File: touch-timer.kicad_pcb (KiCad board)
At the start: 2 copper layers, 23 parts, among them Q2 2N3904, U1 WeMos_D1_mini

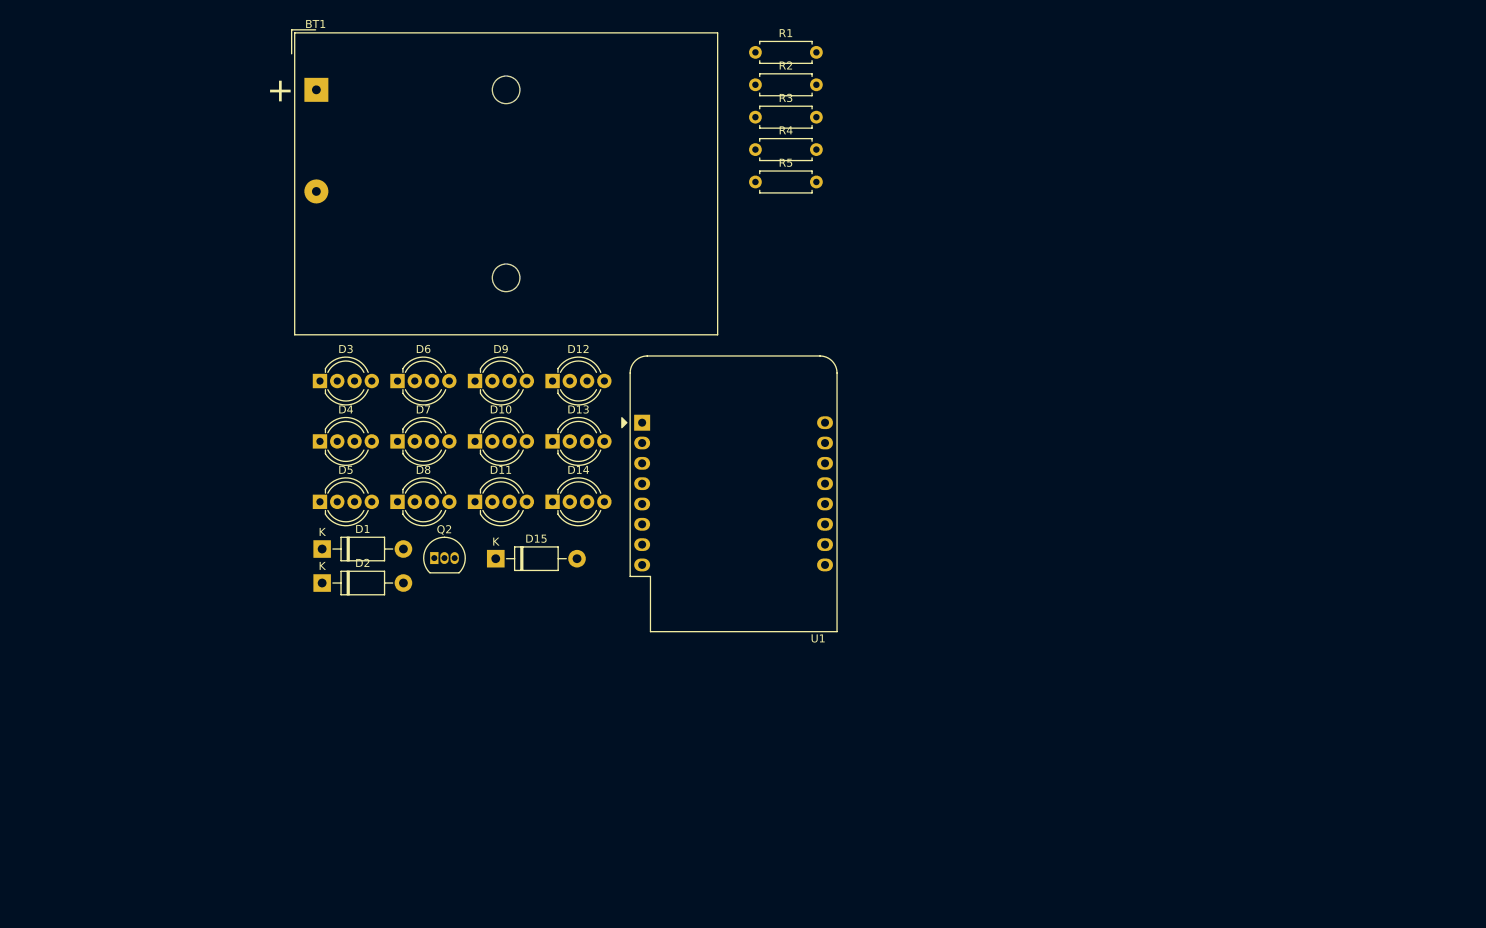
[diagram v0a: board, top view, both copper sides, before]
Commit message: Add Lolin C3 and place the leds in a circular fashion
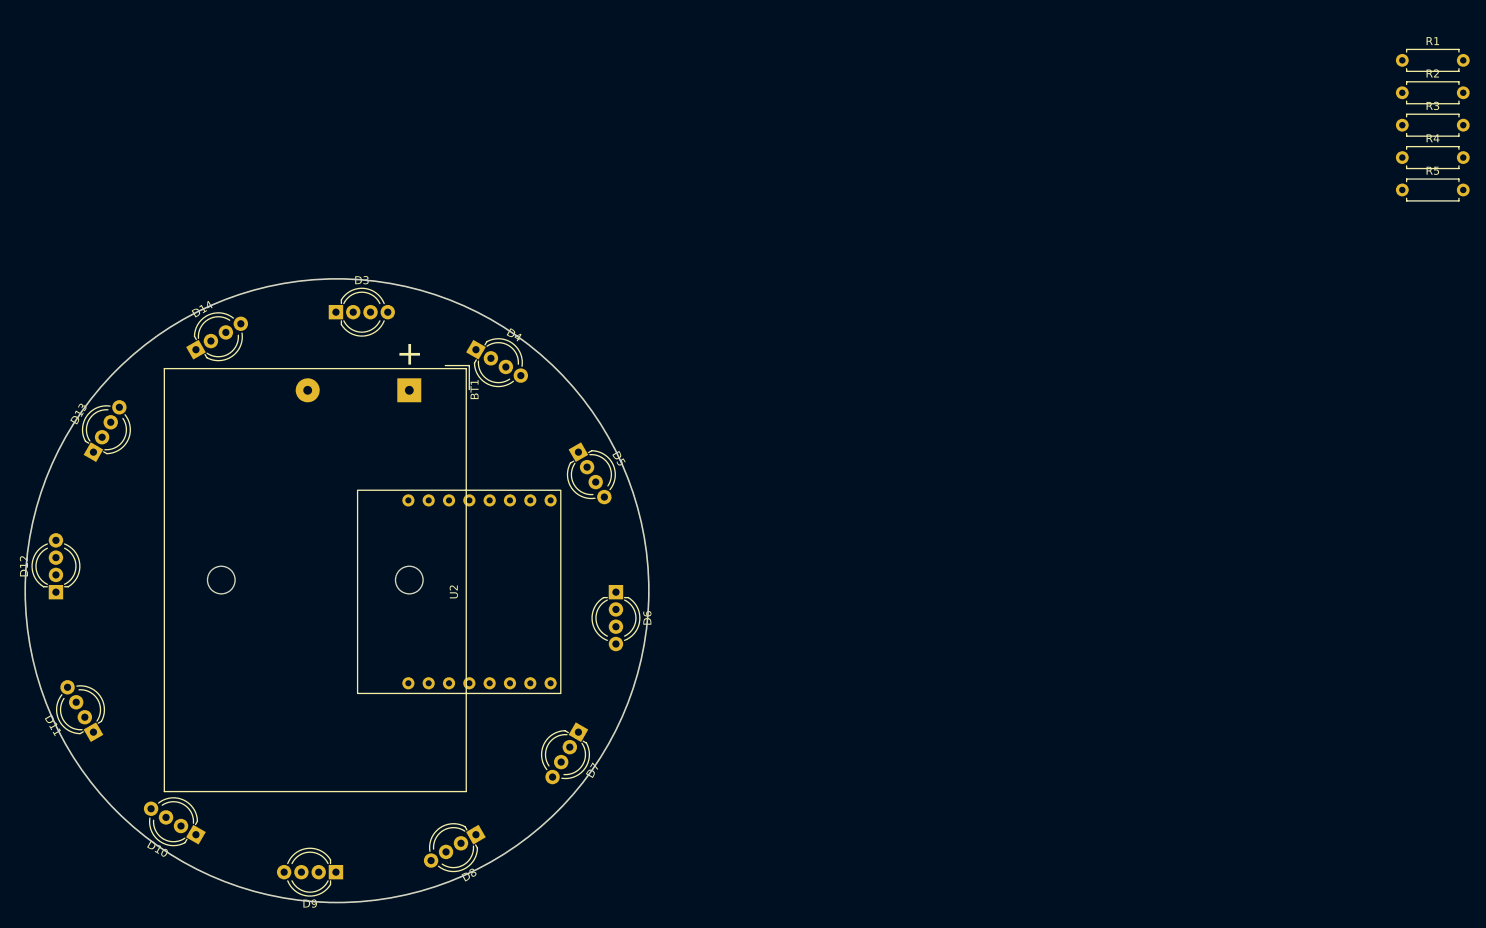
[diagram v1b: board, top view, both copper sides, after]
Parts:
- removed D1, D2: 1N5819, Diode_THT:D_DO-41_SOD81_P10.16mm_Horizontal
- removed D15: 1N4007, Diode_THT:D_DO-41_SOD81_P10.16mm_Horizontal
- removed Q2: 2N3904, Package_TO_SOT_THT:TO-92_Inline
- removed U1: WeMos_D1_mini, Module:WEMOS_D1_mini_light
- added U2: C3 Pico, c3-pico:c3-pico, F.Cu at (115.3, 100.1)
- moved R1 80.9 mm to (233.2, 33.7)
- moved R2 80.9 mm to (233.2, 37.8)
- moved R3 80.9 mm to (233.2, 41.8)
- moved R4 80.9 mm to (233.2, 45.9)
- moved R5 80.9 mm to (233.2, 49.9)
- moved D12 67.5 mm to (64.9, 100.2), turned to 90 degrees
- moved D9 63.8 mm to (99.9, 135.2), turned to 180 degrees
- moved D10 60.3 mm to (82.4, 130.5), turned to 150 degrees
- moved D13 57.4 mm to (69.6, 82.7), turned to 60 degrees
- moved D11 55.7 mm to (69.6, 117.7), turned to 120 degrees
- moved D14 48.5 mm to (82.4, 69.9), turned to 30 degrees
- moved D7 42.8 mm to (130.2, 117.7), turned to -120 degrees
- moved D8 42.7 mm to (117.4, 130.5), turned to -150 degrees
- moved BT1 39.3 mm to (109.0, 74.9), turned to -90 degrees
- moved D6 38.0 mm to (134.9, 100.2), turned to -90 degrees
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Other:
- board outline added: 78 x 78 mm
